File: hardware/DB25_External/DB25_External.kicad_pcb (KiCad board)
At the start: 2 copper layers, 49 x 53.2 mm, 64 parts, among them J2 DB25_Male_MountingHoles, U1 74HC14, U3 AMS1117-2.85, U4 LVT245, U5 LVT125, U6 LVT125, U7 LVT125, U9 LVT245

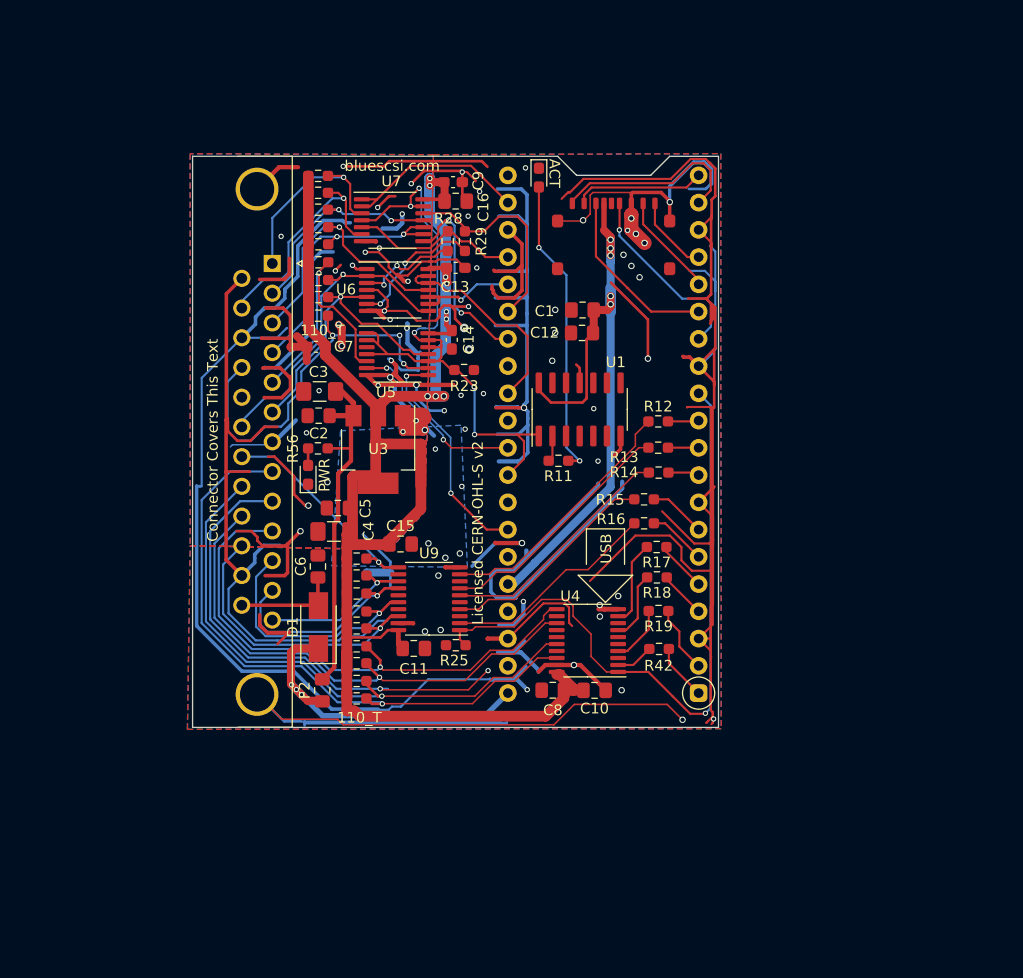
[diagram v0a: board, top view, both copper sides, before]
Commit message: My version sent to Aisler, pico under the PCB
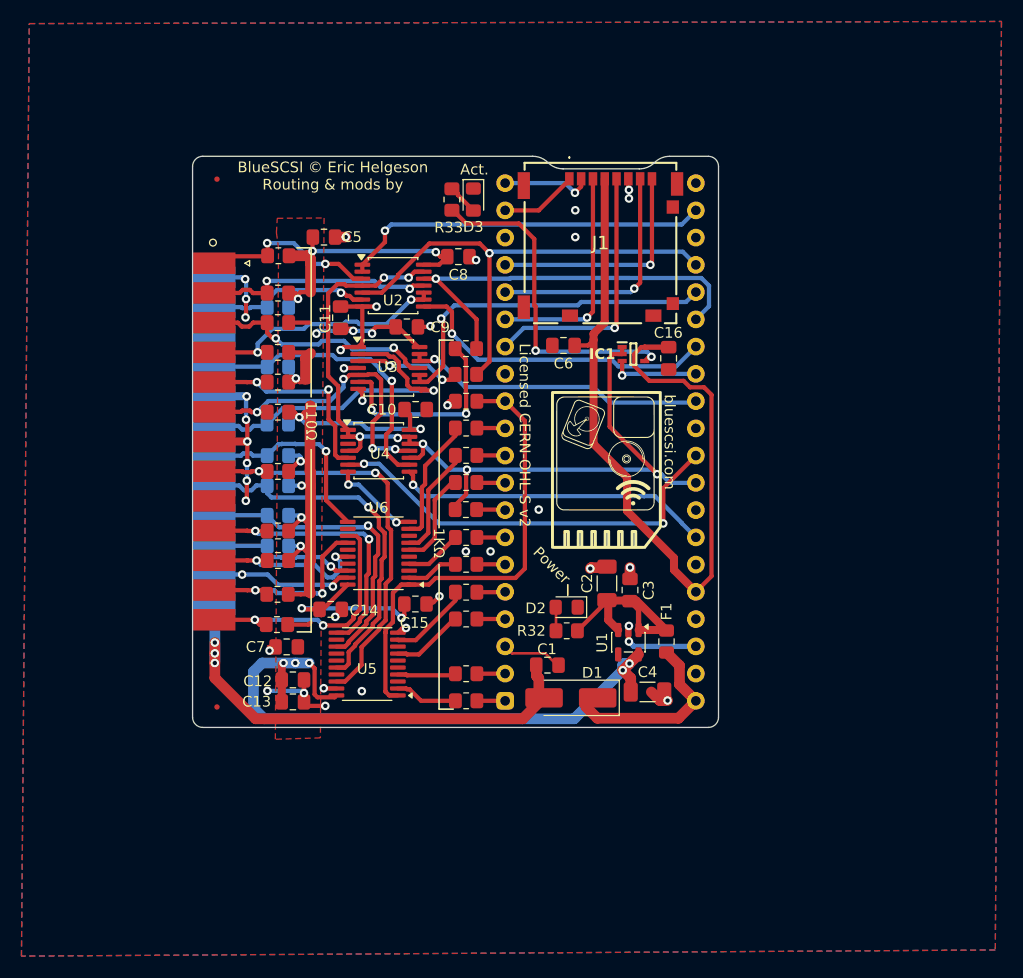
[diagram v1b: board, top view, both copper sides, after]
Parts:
- removed R36, R37, R38, R39, R40: R, Resistor_SMD:R_0603_1608Metric_Pad0.98x0.95mm_HandSolder
- removed SD2: MicroSD-TF-06, Library:TF-06_MicroSD
- removed the U3 at (117.3, 101.4)
- added FID1: Fiducial, Fiducial:Fiducial_0.5mm_Mask1.5mm, F.Cu at (102.3, 125.4)
- added FID2: Fiducial, Fiducial:Fiducial_0.5mm_Mask1.5mm, F.Cu at (102.3, 76.2)
- added G***: LOGO, LOGO, F.Cu at (138.6, 103.3)
- added IC1: MC74VHC1G132DFT1G, SOT65P210X110-5N:SOT65P210X110-5N, F.Cu at (141.1, 92.5)
- added J1: MEM2090-00-145-00-A, Library:MEM20900014500A, F.Cu at (138.0, 82.2)
- added R11: 110, Resistor_SMD:R_0805_2012Metric_Pad1.20x1.40mm_HandSolder, F.Cu at (108.0, 83.3)
- added R12: 110, Resistor_SMD:R_0805_2012Metric_Pad1.20x1.40mm_HandSolder, B.Cu at (108.0, 88.1)
- added R13: 110, Resistor_SMD:R_0805_2012Metric_Pad1.20x1.40mm_HandSolder, F.Cu at (108.0, 86.8)
- added R14: 110, Resistor_SMD:R_0805_2012Metric_Pad1.20x1.40mm_HandSolder, F.Cu at (108.0, 97.9)
- added R5: 110, Resistor_SMD:R_0805_2012Metric_Pad1.20x1.40mm_HandSolder, B.Cu at (108.0, 110.4)
- C1: renamed from C6; footprint Capacitor_SMD:C_0805_2012Metric_Pad1.15x1.40mm_HandSolder -> Capacitor_SMD:C_0805_2012Metric_Pad1.18x1.45mm_HandSolder
- C10: renamed from C14; footprint Capacitor_SMD:C_0603_1608Metric_Pad1.08x0.95mm_HandSolder -> Capacitor_SMD:C_0805_2012Metric_Pad1.18x1.45mm_HandSolder
- C2: renamed from C3; footprint Capacitor_SMD:C_1206_3216Metric_Pad1.42x1.75mm_HandSolder -> Capacitor_SMD:C_1206_3216Metric_Pad1.33x1.80mm_HandSolder
- C3: renamed from C2; footprint Capacitor_SMD:C_0805_2012Metric_Pad1.15x1.40mm_HandSolder -> Capacitor_SMD:C_0805_2012Metric_Pad1.18x1.45mm_HandSolder
- C4: footprint Capacitor_SMD:C_1206_3216Metric_Pad1.42x1.75mm_HandSolder -> Capacitor_SMD:C_1206_3216Metric_Pad1.33x1.80mm_HandSolder
- C5: footprint Capacitor_SMD:C_0805_2012Metric_Pad1.15x1.40mm_HandSolder -> Capacitor_SMD:C_0805_2012Metric_Pad1.18x1.45mm_HandSolder
- C6: renamed from C12; footprint Capacitor_SMD:C_0805_2012Metric_Pad1.15x1.40mm_HandSolder -> Capacitor_SMD:C_0805_2012Metric_Pad1.18x1.45mm_HandSolder
- C7: footprint Capacitor_SMD:C_0603_1608Metric_Pad1.08x0.95mm_HandSolder -> Capacitor_SMD:C_0805_2012Metric_Pad1.18x1.45mm_HandSolder
- C8: renamed from C9; footprint Capacitor_SMD:C_0603_1608Metric_Pad1.08x0.95mm_HandSolder -> Capacitor_SMD:C_0805_2012Metric_Pad1.18x1.45mm_HandSolder
- C9: renamed from C13; footprint Capacitor_SMD:C_0603_1608Metric_Pad1.08x0.95mm_HandSolder -> Capacitor_SMD:C_0805_2012Metric_Pad1.18x1.45mm_HandSolder
- D1: footprint Diode_SMD:D_SMA -> Diode_SMD:D_SMA_Handsoldering
- D2: renamed from D3; footprint LED_SMD:LED_0603_1608Metric_Pad1.05x0.95mm_HandSolder -> LED_SMD:LED_0805_2012Metric_Pad1.15x1.40mm_HandSolder
- D3: renamed from D2; footprint LED_SMD:LED_0603_1608Metric_Pad1.05x0.95mm_HandSolder -> LED_SMD:LED_0805_2012Metric_Pad1.15x1.40mm_HandSolder
- J2: footprint Connector_Dsub:DSUB-25_Male_Horizontal_P2.77x2.84mm_EdgePinOffset7.70mm_Housed_MountingHolesOffset9.12mm -> Library:DSUB-25_Male_Horizontal_middle_mount
- R1: renamed from R35; value R -> 110; footprint Resistor_SMD:R_0603_1608Metric_Pad0.98x0.95mm_HandSolder -> Resistor_SMD:R_0805_2012Metric_Pad1.20x1.40mm_HandSolder; moved to B.Cu
- R10, R6, R9: value R -> 110; footprint Resistor_SMD:R_0603_1608Metric_Pad0.98x0.95mm_HandSolder -> Resistor_SMD:R_0805_2012Metric_Pad1.20x1.40mm_HandSolder
- R15: renamed from R5; value R -> 110; footprint Resistor_SMD:R_0603_1608Metric_Pad0.98x0.95mm_HandSolder -> Resistor_SMD:R_0805_2012Metric_Pad1.20x1.40mm_HandSolder; moved to B.Cu
- R16: renamed from R4; value R -> 110; footprint Resistor_SMD:R_0603_1608Metric_Pad0.98x0.95mm_HandSolder -> Resistor_SMD:R_0805_2012Metric_Pad1.20x1.40mm_HandSolder
- R17: renamed from R3; value R -> 110; footprint Resistor_SMD:R_0603_1608Metric_Pad0.98x0.95mm_HandSolder -> Resistor_SMD:R_0805_2012Metric_Pad1.20x1.40mm_HandSolder
- R18: renamed from R2; value R -> 110; footprint Resistor_SMD:R_0603_1608Metric_Pad0.98x0.95mm_HandSolder -> Resistor_SMD:R_0805_2012Metric_Pad1.20x1.40mm_HandSolder; moved to B.Cu
- R19: renamed from R23; footprint Resistor_SMD:R_0603_1608Metric_Pad0.98x0.95mm_HandSolder -> Resistor_SMD:R_0805_2012Metric_Pad1.20x1.40mm_HandSolder
- R2: renamed from R34; value R -> 110; footprint Resistor_SMD:R_0603_1608Metric_Pad0.98x0.95mm_HandSolder -> Resistor_SMD:R_0805_2012Metric_Pad1.20x1.40mm_HandSolder
- R20: renamed from R25; footprint Resistor_SMD:R_0603_1608Metric_Pad0.98x0.95mm_HandSolder -> Resistor_SMD:R_0805_2012Metric_Pad1.20x1.40mm_HandSolder
- R21: renamed from R28; footprint Resistor_SMD:R_0603_1608Metric_Pad0.98x0.95mm_HandSolder -> Resistor_SMD:R_0805_2012Metric_Pad1.20x1.40mm_HandSolder
- R22: renamed from R29; footprint Resistor_SMD:R_0603_1608Metric_Pad0.98x0.95mm_HandSolder -> Resistor_SMD:R_0805_2012Metric_Pad1.20x1.40mm_HandSolder
- R23: renamed from R12; footprint Resistor_SMD:R_0603_1608Metric_Pad0.98x0.95mm_HandSolder -> Resistor_SMD:R_0805_2012Metric_Pad1.20x1.40mm_HandSolder
- R24: renamed from R13; footprint Resistor_SMD:R_0603_1608Metric_Pad0.98x0.95mm_HandSolder -> Resistor_SMD:R_0805_2012Metric_Pad1.20x1.40mm_HandSolder
- R25: renamed from R14; footprint Resistor_SMD:R_0603_1608Metric_Pad0.98x0.95mm_HandSolder -> Resistor_SMD:R_0805_2012Metric_Pad1.20x1.40mm_HandSolder
- R26: renamed from R15; footprint Resistor_SMD:R_0603_1608Metric_Pad0.98x0.95mm_HandSolder -> Resistor_SMD:R_0805_2012Metric_Pad1.20x1.40mm_HandSolder
- R27: renamed from R16; footprint Resistor_SMD:R_0603_1608Metric_Pad0.98x0.95mm_HandSolder -> Resistor_SMD:R_0805_2012Metric_Pad1.20x1.40mm_HandSolder
- R28: renamed from R17; footprint Resistor_SMD:R_0603_1608Metric_Pad0.98x0.95mm_HandSolder -> Resistor_SMD:R_0805_2012Metric_Pad1.20x1.40mm_HandSolder
- R29: renamed from R18; footprint Resistor_SMD:R_0603_1608Metric_Pad0.98x0.95mm_HandSolder -> Resistor_SMD:R_0805_2012Metric_Pad1.20x1.40mm_HandSolder
- R3: renamed from R33; value R -> 110; footprint Resistor_SMD:R_0603_1608Metric_Pad0.98x0.95mm_HandSolder -> Resistor_SMD:R_0805_2012Metric_Pad1.20x1.40mm_HandSolder
- R30: renamed from R19; footprint Resistor_SMD:R_0603_1608Metric_Pad0.98x0.95mm_HandSolder -> Resistor_SMD:R_0805_2012Metric_Pad1.20x1.40mm_HandSolder
- R31: renamed from R42; footprint Resistor_SMD:R_0603_1608Metric_Pad0.98x0.95mm_HandSolder -> Resistor_SMD:R_0805_2012Metric_Pad1.20x1.40mm_HandSolder
- R32: renamed from R56; footprint Resistor_SMD:R_0603_1608Metric_Pad0.98x0.95mm_HandSolder -> Resistor_SMD:R_0805_2012Metric_Pad1.20x1.40mm_HandSolder
- R33: renamed from R11; footprint Resistor_SMD:R_0603_1608Metric_Pad0.98x0.95mm_HandSolder -> Resistor_SMD:R_0805_2012Metric_Pad1.20x1.40mm_HandSolder
- R4: renamed from R1; value R -> 110; footprint Resistor_SMD:R_0603_1608Metric_Pad0.98x0.95mm_HandSolder -> Resistor_SMD:R_0805_2012Metric_Pad1.20x1.40mm_HandSolder
- R7, R8: value R -> 110; footprint Resistor_SMD:R_0603_1608Metric_Pad0.98x0.95mm_HandSolder -> Resistor_SMD:R_0805_2012Metric_Pad1.20x1.40mm_HandSolder; moved to B.Cu
- RP1: moved to B.Cu
- U1: value 74HC14 -> MIC5219-2.85YM5; footprint Package_SO:SOIC-14_3.9x8.7mm_P1.27mm -> Package_TO_SOT_SMD:SOT-23-5
- moved C3 33.3 mm to (140.8, 114.5), turned to 90 degrees
- moved C4 32.8 mm to (142.4, 124.0), turned to 0 degrees
- moved F1 32.4 mm to (144.2, 119.3)
- moved C2 32.2 mm to (138.7, 113.9), turned to 90 degrees
- moved R7 31.9 mm to (108.0, 107.5), turned to 180 degrees
- moved R32 28.8 mm to (134.9, 118.3)
- moved R6 28.6 mm to (108.0, 109.0), turned to 180 degrees
- moved C13 28.1 mm to (109.4, 124.9)
- moved C7 28.1 mm to (108.8, 119.8)
- moved R8 27.6 mm to (108.0, 104.8), turned to 180 degrees
- moved D2 27.1 mm to (134.9, 116.1), turned to 180 degrees
- moved R33 26.3 mm to (124.2, 78.1), turned to 90 degrees
- moved C5 25.3 mm to (112.3, 81.6), turned to 0 degrees
- moved R9 24.7 mm to (108.0, 103.4), turned to 180 degrees
- moved D1 24.4 mm to (135.3, 124.5), turned to 180 degrees
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- renumbered C16 to C11, C8 to C12, C10 to C13, C11 to C14, C1 to C16, F2 to F1, U7 to U2, U6 to U3, U5 to U4, U4 to U5, U9 to U6
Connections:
- R10 pad 2: BSY -> IO
- R33 pad 1: Net-(R11-Pad1) -> Net-(IC1-Y)
- R6 pad 2: IO -> DB3
- R7 pad 2: REQ -> DB2
- R8 pad 2: CD -> DB1
- R9 pad 2: MSG -> DB0
- U1 pad 1: oBSY -> +5F
- U1 pad 2: Net-(R11-Pad1) -> GND
- U1 pad 3: GND -> +5F
- U1 pad 5: GND -> +2V8
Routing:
- net GND: track 864.6 -> 105.1 mm, vias 75 -> 43
- net +5V: track 9.80 -> 45.3 mm, vias 0 -> 3
- net Net-(IC1-Y): track 0.00 -> 31.1 mm, vias 0 -> 2
- net oCD_iSEL: track 15.7 -> 45.8 mm, vias 0 -> 1
- net Net-(D3-A): track 28.3 -> 2.91 mm, vias 2 -> 0
- net DB3: track 51.1 -> 26.5 mm, vias 1 -> 2
- net +2V8: track 161.7 -> 185.4 mm, vias 9 -> 20
- net oSEL: track 9.81 -> 32.7 mm
- net oBSY: track 61.5 -> 83.2 mm, vias 5 -> 7
- net iACK: track 17.8 -> 39.3 mm
- net DB2: track 49.2 -> 28.6 mm
- net DB0: track 58.8 -> 38.6 mm, vias 1 -> 2
- net DB1: track 53.8 -> 33.9 mm
- net DBPTr: track 62.4 -> 43.2 mm, vias 1 -> 0
- net oMSG_iBSY: track 20.2 -> 38.7 mm, vias 0 -> 1
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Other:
- outline, holes or cut-outs redrawn
- board text added: "110Ω"
- board text added: "1KΩ"
- board text added: "Act."
- board text added: "BlueSCSI © Eric Helgeson Routing & mods by"
- board text added: "Power"
- board text added: "Your Pico should cover this text"
- board text added: "fabien@acathla.tk"
- board text removed: "110_T"
- board text removed: "ACT"
- board text removed: "BlueSCSI © Eric Helgeson PCB © Tech by Androda, LLC"
- board text removed: "Connector Covers This Text"
- board text removed: "Manufactured By:"
- board text removed: "PWR"

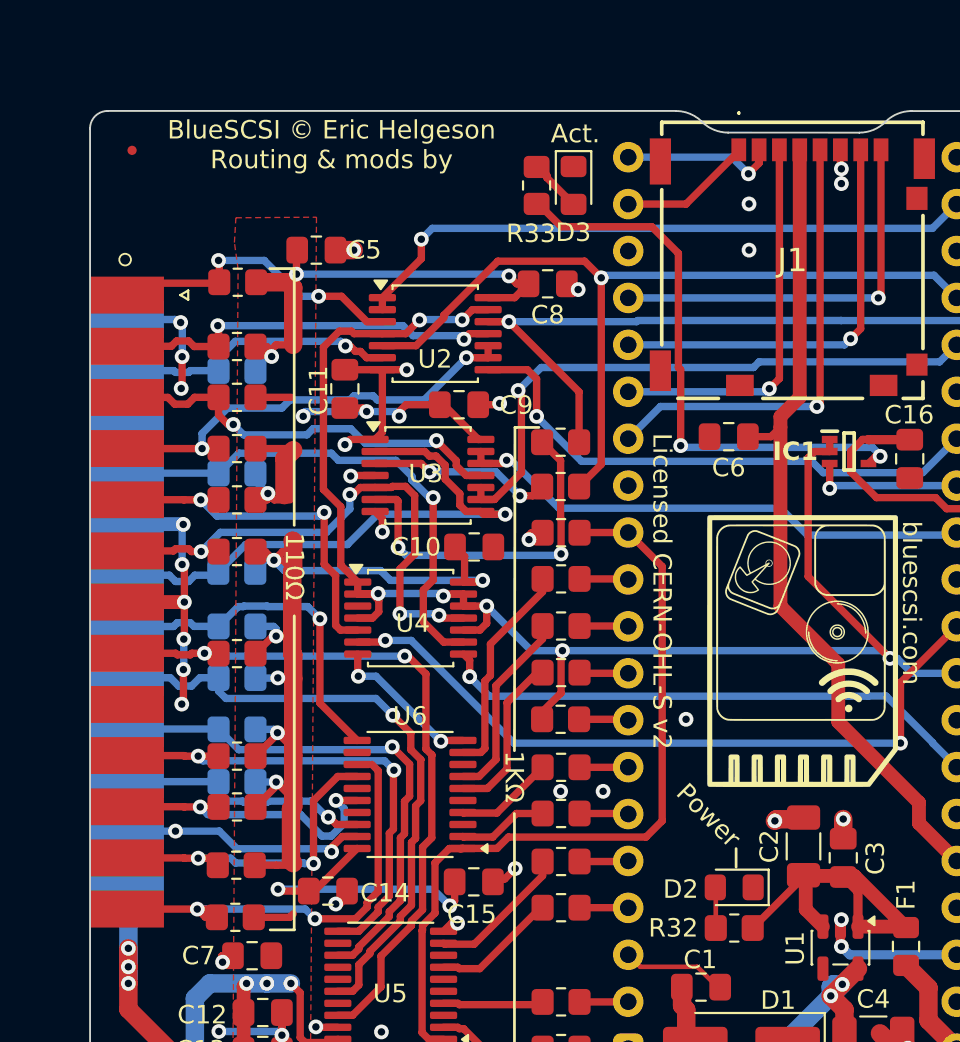
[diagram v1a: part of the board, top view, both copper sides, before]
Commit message: Via moved out of pad and original (c) text added
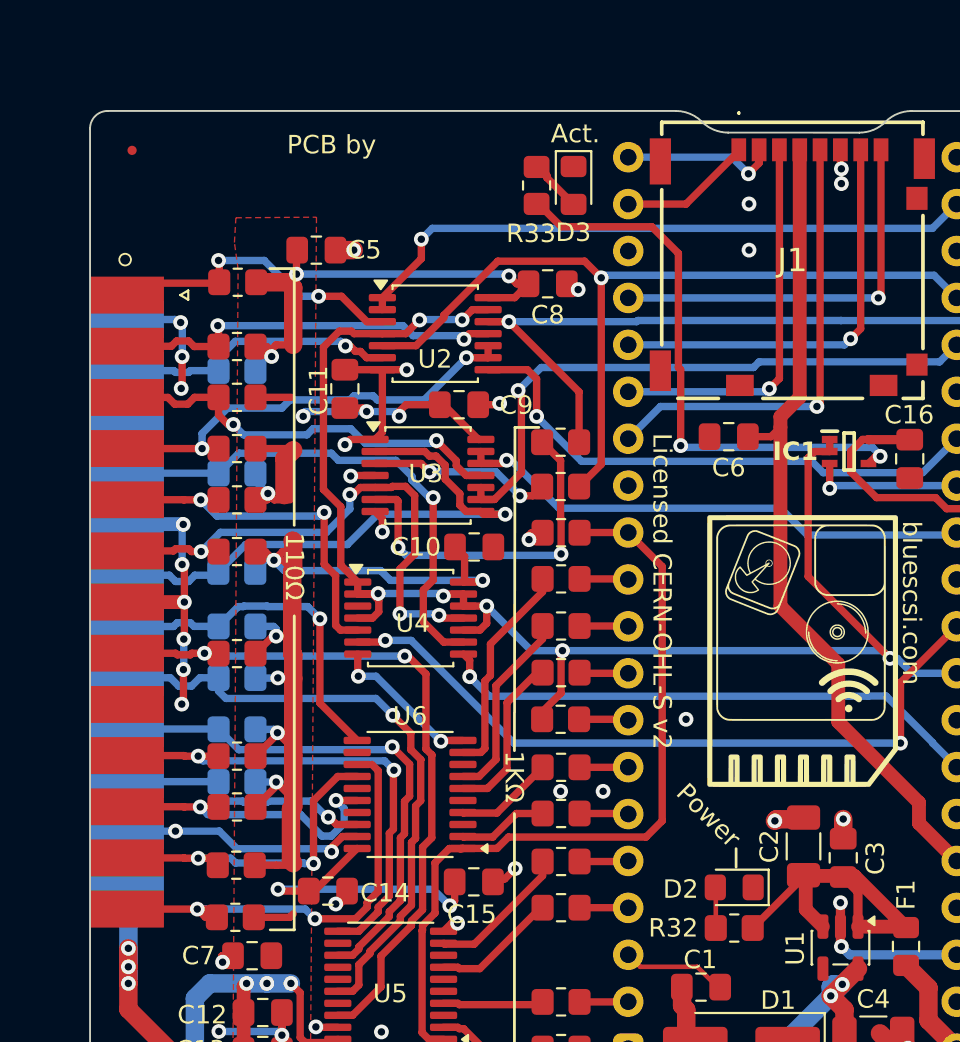
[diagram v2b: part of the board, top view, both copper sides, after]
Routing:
- net GND: track 105.1 -> 106.0 mm
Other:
- board text added: "BlueSCSI © Eric Helgeson PCB © Tech by Androda, LLC"
- board text added: "PCB by"
- board text removed: "BlueSCSI © Eric Helgeson Routing & mods by"
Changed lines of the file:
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@@
 	)
 	(gr_text "fabien@acathla.tk"
-		(at 106.5 79 0)
+		(at 106.57 78.1 0)
 		(layer "F.Mask")
 		(effects
@@
 		)
 	)
-	(gr_text "BlueSCSI © Eric Helgeson\nRouting & mods by"
+	(gr_text "PCB by"
 		(at 113.1 75.9 0)
 		(layer "F.SilkS")
@@
 		)
 	)
+	(gr_text "BlueSCSI © Eric Helgeson\nPCB © Tech by Androda, LLC"
+		(at 119.72 110.34 90)
+		(layer "B.SilkS")
+		(effects
+			(font
+				(size 1 1)
+				(thickness 0.15)
+			)
+			(justify mirror)
+		)
+	)
 	(gr_text "BlueSCSI V2 - 2024.01a\nLicensed under CERN-OHL-S v2\nhttps://ohwr.org/cern_ohl_s_v2.txt"
 		(at 124.9 110.8 90)
@@
 	)
 	(segment
+		(start 140.649999 118.225)
+		(end 140.65 116.93)
+		(width 0.5)
+		(layer "F.Cu")
+		(net 1)
+	)
+	(segment
 		(start 115.85 91.4575)
 		(end 115.4575 91.85)
@@
 		(end 105.13 98.74)
 		(width 0.4)
-		(layer "F.Cu")
-		(net 1)
-	)
-	(segment
-		(start 140.649999 118.225)
-		(end 140.649999 117.897503)
-		(width 0.5)
 		(layer "F.Cu")
 		(net 1)
@@
 	)
 	(segment
-		(start 140.649999 117.897503)
-		(end 140.7 117.847502)
-		(width 0.5)
-		(layer "F.Cu")
-		(net 1)
-	)
-	(segment
 		(start 107.144821 120.095456)
 		(end 107.199365 120.15)
@@
 	)
 	(via
-		(at 140.7 117.847502)
-		(size 0.8)
-		(drill 0.4)
+		(at 140.65 116.93)
+		(size 0.8)
+		(drill 0.4)

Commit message: Clean up
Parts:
- moved G*** 0.24 mm to (138.7, 103.1)
- moved C12 0.24 mm to (109.4, 122.6)
- moved C13 0.11 mm to (109.3, 125.0)
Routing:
- net GND: track 106.0 -> 104.4 mm
- net oREQ: track 34.5 -> 33.8 mm
- net +2V8: track 185.4 -> 186.0 mm
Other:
- board text added: "BlueSCSI © Eric Helgeson PCB © Tech by Androda, LLC Modifications by fabien@acathla.tk Licensed under CERN-OHL-S v2 https://ohwr.org/cern_ohl_s_v2.txt This source is distributed WITHOUT ANY EXPRESS OR IMPLIED WARRANTY, INCLUDING OF MERCHANTABILITY, SATISFACTORY QUALITY AND FITNESS FOR A PARTICULAR PURPOSE. Please see the CERN-OHL-S v2 for applicable conditions. As per CERN-OHL-S v2 section 4, sho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"
- board text added: "PCB mods by"
- board text added: "https://github.com/Acathla-fr/BlueSCSI-v2"
- board text removed: "BlueSCSI © Eric Helgeson PCB © Tech by Androda, LLC Licensed under CERN-OHL-S v2 https://ohwr.org/cern_ohl_s_v2.txt This source is distributed WITHOUT ANY EXPRESS OR IMPLIED WARRANTY, INCLUDING OF MERCHANTABILITY, SATISFACTORY QUALITY AND FITNESS FOR A PARTICULAR PURPOSE. Please see the CERN-OHL-S v2 for applicable conditions. As per CERN-OHL-S v2 section 4, should You produce hardware based on t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"
- board text removed: "PCB by"
